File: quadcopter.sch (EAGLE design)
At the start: 66 parts, among them J1 AVR_SPI_PRG_6NS, M1 MOTOR_PADS, M2 MOTOR_PADS, M3 MOTOR_PADS, M4 MOTOR_PADS, Q1 MOSFET_SOT-23, Q2 MOSFET_SOT-23, Q3 MOSFET_SOT-23, Q4 MOSFET_SOT-23, SW1 PUSHBUTTON_SMD-VERTICAL-1, U1 ATMEGA128RFA1, U2 IMU_LSM9DS1TR, Y1 16MHz

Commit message: Rename N0 net
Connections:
- net N$1 renamed C6
- net N$10 renamed M2
- net N$11 renamed C22
- net N$12 renamed BATT1
- net N$13 renamed M1
- net N$14 renamed M3
- net N$15 renamed C9
- net N$16 renamed D6
- net N$17 renamed C21
- net N$18 renamed C13
- net N$19 renamed C14
- net N$2 renamed C5
- net N$20 renamed C23
- net N$21 renamed M4
- net N$22 renamed D7
- net N$23 renamed C24
- net N$3 renamed RFP
- net N$4 renamed RFN
- net N$5 renamed C1
- net N$6 renamed C4
- net N$7 renamed C2
- net N$8 renamed C3
- net N$9 renamed D5
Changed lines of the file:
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@@
 </segment>
 </net>
-<net name="N$3" class="0">
+<net name="RFP" class="0">
 <segment>
 <pinref part="U1" gate="G$1" pin="RFP"/>
@@
 </segment>
 </net>
-<net name="N$4" class="0">
-<segment>
-<pinref part="U1" gate="G$1" pin="RFN"/>
-<wire x1="200.66" y1="157.48" x2="218.44" y2="157.48" width="0.1524" layer="91"/>
-<wire x1="218.44" y1="157.48" x2="218.44" y2="149.86" width="0.1524" layer="91"/>
-<wire x1="218.44" y1="149.86" x2="236.22" y2="149.86" width="0.1524" layer="91"/>
-<wire x1="236.22" y1="149.86" x2="236.22" y2="152.4" width="0.1524" layer="91"/>
-<pinref part="B1" gate="G$1" pin="OUT2"/>
-</segment>
-</net>
-<net name="N$5" class="0">
+<net name="C1" class="0">
 <segment>
 <pinref part="B1" gate="G$1" pin="GND@2"/>
@@
 </segment>
 </net>
-<net name="N$7" class="0">
+<net name="C2" class="0">
 <segment>
 <pinref part="B1" gate="G$1" pin="IN"/>
@@
 </segment>
 </net>
-<net name="N$1" class="0">
+<net name="C6" class="0">
 <segment>
 <pinref part="U1" gate="G$1" pin="AVDD"/>
@@
 </segment>
 </net>
-<net name="N$2" class="0">
+<net name="C5" class="0">
 <segment>
 <pinref part="U1" gate="G$1" pin="DVDD"/>
@@
 </segment>
 </net>
-<net name="N$6" class="0">
+<net name="C4" class="0">
 <segment>
 <pinref part="U1" gate="G$1" pin="XTAL1"/>
@@
 </segment>
 </net>
-<net name="N$8" class="0">
+<net name="C3" class="0">
 <segment>
 <pinref part="U1" gate="G$1" pin="XTAL2"/>
@@
 </segment>
 </net>
-<net name="N$15" class="0">
+<net name="C9" class="0">
 <segment>
 <pinref part="JP1" gate="G$1" pin="1"/>
@@
 </segment>
 </net>
-<net name="N$18" class="0">
+<net name="C13" class="0">
 <segment>
 <pinref part="U2" gate="G$1" pin="CAP"/>
@@
 </segment>
 </net>
-<net name="N$19" class="0">
+<net name="C14" class="0">
 <segment>
 <pinref part="U2" gate="G$1" pin="C1"/>
@@
 </segment>
 </net>
-<net name="N$12" class="0">
+<net name="BATT1" class="0">
 <segment>
 <pinref part="J2" gate="G$1" pin="1"/>
@@
 </segment>
 </net>
-<net name="N$13" class="0">
+<net name="M1" class="0">
 <segment>
 <pinref part="M1" gate="G$1" pin="V-"/>
@@
 </segment>
 </net>
-<net name="N$17" class="0">
+<net name="C21" class="0">
 <segment>
 <pinref part="Q1" gate="G$1" pin="G"/>
@@
 </segment>
 </net>
-<net name="N$10" class="0">
+<net name="M2" class="0">
 <segment>
 <pinref part="M2" gate="G$1" pin="V-"/>
@@
 </segment>
 </net>
-<net name="N$11" class="0">
+<net name="C22" class="0">
 <segment>
 <pinref part="Q2" gate="G$1" pin="G"/>
@@
 </segment>
 </net>
-<net name="N$14" class="0">
+<net name="M3" class="0">
 <segment>
 <pinref part="M3" gate="G$1" pin="V-"/>
@@
 </segment>
 </net>
-<net name="N$20" class="0">
+<net name="C23" class="0">
 <segment>
 <pinref part="Q3" gate="G$1" pin="G"/>
@@
 </segment>
 </net>
-<net name="N$21" class="0">
+<net name="M4" class="0">
 <segment>
 <pinref part="M4" gate="G$1" pin="V-"/>
@@
 </segment>
 </net>
-<net name="N$23" class="0">
+<net name="C24" class="0">
 <segment>
 <pinref part="Q4" gate="G$1" pin="G"/>
@@
 </segment>
 </net>
-<net name="N$9" class="0">
+<net name="D5" class="0">
 <segment>
 <pinref part="R12" gate="G$1" pin="1"/>
@@
 </segment>
 </net>
-<net name="N$16" class="0">
+<net name="D6" class="0">
 <segment>
 <pinref part="R13" gate="G$1" pin="1"/>
@@
 </segment>
 </net>
-<net name="N$22" class="0">
+<net name="D7" class="0">
 <segment>
 <pinref part="R14" gate="G$1" pin="1"/>
@@
 </segment>
 </net>
+<net name="RFN" class="0">
+<segment>
+<pinref part="U1" gate="G$1" pin="RFN"/>
+<wire x1="200.66" y1="157.48" x2="218.44" y2="157.48" width="0.1524" layer="91"/>
+<wire x1="218.44" y1="157.48" x2="218.44" y2="149.86" width="0.1524" layer="91"/>
+<wire x1="218.44" y1="149.86" x2="236.22" y2="149.86" width="0.1524" layer="91"/>
+<pinref part="B1" gate="G$1" pin="OUT2"/>
+<wire x1="236.22" y1="149.86" x2="236.22" y2="152.4" width="0.1524" layer="91"/>
+</segment>
+</net>

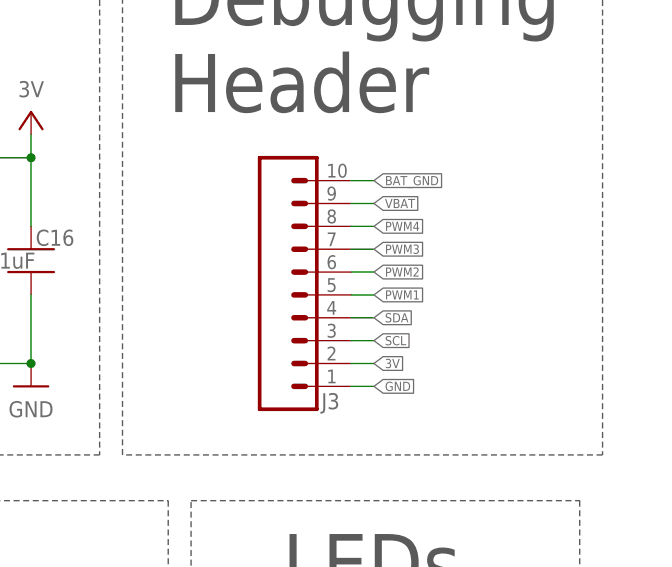
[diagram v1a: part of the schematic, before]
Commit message: Placed some parts on the board
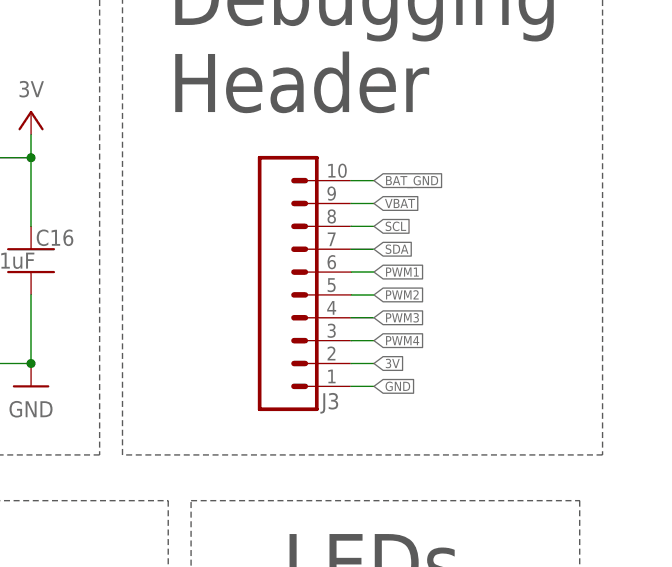
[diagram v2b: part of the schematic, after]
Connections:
- net PWM1: now also J3.6; no longer J3.5
- net PWM2: now also J3.5; no longer J3.6
- net PWM3: now also J3.4; no longer J3.7
- net PWM4: now also J3.3; no longer J3.8
- net SCL: now also J3.8; no longer J3.3
- net SDA: now also J3.7; no longer J3.4
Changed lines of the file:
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@@
 </segment>
 <segment>
-<pinref part="J3" gate="G$1" pin="8"/>
-<wire x1="375.92" y1="187.96" x2="378.46" y2="187.96" width="0.1524" layer="91"/>
-<label x="378.46" y="187.96" size="1.016" layer="95" xref="yes"/>
+<pinref part="J3" gate="G$1" pin="3"/>
+<wire x1="375.92" y1="175.26" x2="378.46" y2="175.26" width="0.1524" layer="91"/>
+<label x="378.46" y="175.26" size="1.016" layer="95" xref="yes"/>
 </segment>
 </net>
@@
 </segment>
 <segment>
-<pinref part="J3" gate="G$1" pin="3"/>
-<wire x1="375.92" y1="175.26" x2="378.46" y2="175.26" width="0.1524" layer="91"/>
-<label x="378.46" y="175.26" size="1.016" layer="95" xref="yes"/>
+<pinref part="J3" gate="G$1" pin="8"/>
+<wire x1="375.92" y1="187.96" x2="378.46" y2="187.96" width="0.1524" layer="91"/>
+<label x="378.46" y="187.96" size="1.016" layer="95" xref="yes"/>
 </segment>
 </net>
@@
 </segment>
 <segment>
+<pinref part="J3" gate="G$1" pin="7"/>
+<wire x1="375.92" y1="185.42" x2="378.46" y2="185.42" width="0.1524" layer="91"/>
+<label x="378.46" y="185.42" size="1.016" layer="95" xref="yes"/>
+</segment>
+</net>
+<net name="RXD0" class="0">
+<segment>
+<pinref part="U1" gate="G$1" pin="PE0(RXD0/PCINT8)"/>
+<wire x1="144.78" y1="132.08" x2="142.24" y2="132.08" width="0.1524" layer="91"/>
+<label x="142.24" y="132.08" size="1.016" layer="95" rot="R180" xref="yes"/>
+</segment>
+<segment>
+<pinref part="JP1" gate="G$1" pin="3"/>
+<wire x1="157.48" y1="78.74" x2="160.02" y2="78.74" width="0.1524" layer="91"/>
+<label x="160.02" y="78.74" size="1.016" layer="95" xref="yes"/>
+</segment>
+</net>
+<net name="TXD0" class="0">
+<segment>
+<pinref part="U1" gate="G$1" pin="PE1(TXD0)"/>
+<wire x1="144.78" y1="129.54" x2="142.24" y2="129.54" width="0.1524" layer="91"/>
+<label x="142.24" y="129.54" size="1.016" layer="95" rot="R180" xref="yes"/>
+</segment>
+<segment>
+<pinref part="JP1" gate="G$1" pin="2"/>
+<wire x1="157.48" y1="81.28" x2="160.02" y2="81.28" width="0.1524" layer="91"/>
+<label x="160.02" y="81.28" size="1.016" layer="95" xref="yes"/>
+</segment>
+</net>
+<net name="PWM3" class="0">
+<segment>
+<pinref part="U1" gate="G$1" pin="PE5(OC3C/INT5)"/>
+<wire x1="144.78" y1="119.38" x2="142.24" y2="119.38" width="0.1524" layer="91"/>
+<label x="142.24" y="119.38" size="1.016" layer="95" rot="R180" xref="yes"/>
+</segment>
+<segment>
+<pinref part="R8" gate="G$1" pin="1"/>
+<wire x1="38.1" y1="116.84" x2="35.56" y2="116.84" width="0.1524" layer="91"/>
+<label x="35.56" y="116.84" size="1.016" layer="95" rot="R180" xref="yes"/>
+</segment>
+<segment>
 <pinref part="J3" gate="G$1" pin="4"/>
 <wire x1="375.92" y1="177.8" x2="378.46" y2="177.8" width="0.1524" layer="91"/>
 <label x="378.46" y="177.8" size="1.016" layer="95" xref="yes"/>
-</segment>
-</net>
-<net name="RXD0" class="0">
-<segment>
-<pinref part="U1" gate="G$1" pin="PE0(RXD0/PCINT8)"/>
-<wire x1="144.78" y1="132.08" x2="142.24" y2="132.08" width="0.1524" layer="91"/>
-<label x="142.24" y="132.08" size="1.016" layer="95" rot="R180" xref="yes"/>
-</segment>
-<segment>
-<pinref part="JP1" gate="G$1" pin="3"/>
-<wire x1="157.48" y1="78.74" x2="160.02" y2="78.74" width="0.1524" layer="91"/>
-<label x="160.02" y="78.74" size="1.016" layer="95" xref="yes"/>
-</segment>
-</net>
-<net name="TXD0" class="0">
-<segment>
-<pinref part="U1" gate="G$1" pin="PE1(TXD0)"/>
-<wire x1="144.78" y1="129.54" x2="142.24" y2="129.54" width="0.1524" layer="91"/>
-<label x="142.24" y="129.54" size="1.016" layer="95" rot="R180" xref="yes"/>
-</segment>
-<segment>
-<pinref part="JP1" gate="G$1" pin="2"/>
-<wire x1="157.48" y1="81.28" x2="160.02" y2="81.28" width="0.1524" layer="91"/>
-<label x="160.02" y="81.28" size="1.016" layer="95" xref="yes"/>
-</segment>
-</net>
-<net name="PWM3" class="0">
-<segment>
-<pinref part="U1" gate="G$1" pin="PE5(OC3C/INT5)"/>
-<wire x1="144.78" y1="119.38" x2="142.24" y2="119.38" width="0.1524" layer="91"/>
-<label x="142.24" y="119.38" size="1.016" layer="95" rot="R180" xref="yes"/>
-</segment>
-<segment>
-<pinref part="R8" gate="G$1" pin="1"/>
-<wire x1="38.1" y1="116.84" x2="35.56" y2="116.84" width="0.1524" layer="91"/>
-<label x="35.56" y="116.84" size="1.016" layer="95" rot="R180" xref="yes"/>
-</segment>
-<segment>
-<pinref part="J3" gate="G$1" pin="7"/>
-<wire x1="375.92" y1="185.42" x2="378.46" y2="185.42" width="0.1524" layer="91"/>
-<label x="378.46" y="185.42" size="1.016" layer="95" xref="yes"/>
 </segment>
 </net>
@@
 </segment>
 <segment>
-<pinref part="J3" gate="G$1" pin="5"/>
-<wire x1="375.92" y1="180.34" x2="378.46" y2="180.34" width="0.1524" layer="91"/>
-<label x="378.46" y="180.34" size="1.016" layer="95" xref="yes"/>
+<pinref part="J3" gate="G$1" pin="6"/>
+<wire x1="375.92" y1="182.88" x2="378.46" y2="182.88" width="0.1524" layer="91"/>
+<label x="378.46" y="182.88" size="1.016" layer="95" xref="yes"/>
 </segment>
 </net>
@@
 </segment>
 <segment>
-<pinref part="J3" gate="G$1" pin="6"/>
-<wire x1="375.92" y1="182.88" x2="378.46" y2="182.88" width="0.1524" layer="91"/>
-<label x="378.46" y="182.88" size="1.016" layer="95" xref="yes"/>
-</segment>
-</net>
+<pinref part="J3" gate="G$1" pin="5"/>
+<wire x1="375.92" y1="180.34" x2="378.46" y2="180.34" width="0.1524" layer="91"/>
+<label x="378.46" y="180.34" size="1.016" layer="95" xref="yes"/>
+</segment>
+</net>

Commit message: Finished board design
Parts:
- added V1, V10, V11, V12, V13, V14, V15, V16, V17, V18, V19, V2, V20, V21, V22, V23, V24, V25, V26, V27, V28, V29, V3, V30, V31, V32, V33, V4, V5, V6, V7, V8, V9: (no value), quadparts_prebuilt:LOCKED-VIA-0.254
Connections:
- net 3V: now also V1.N, V2.N, V3.N, V32.N, V4.N
- net BAT_GND: now also V5.N, V6.N, V7.N, V8.N
- net GND: now also V13.N, V14.N, V15.N, V16.N, V17.N, V18.N, V19.N, V20.N, V21.N, V22.N, V23.N, V24.N, V25.N, V26.N, V27.N, V28.N, V29.N, V30.N, V31.N, V33.N
- net VBAT: now also V10.N, V11.N, V12.N, V9.N
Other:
- note added: "VIAs"
- moved on the sheet: C10, C11, C12, C13, C14, D5, D6, D7, R12, R13, R14, R2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

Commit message: Modified board design
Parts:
- removed V2, V4: (no value), quadparts_prebuilt:LOCKED-VIA-0.254
- added V34: (no value), quadparts_prebuilt:LOCKED-VIA-0.254
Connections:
- net 3V: no longer V2.N, V4.N
- net GND: now also V34.N
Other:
- moved on the sheet: V3, V32
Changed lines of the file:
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@@
 <?xml version="1.0" encoding="utf-8"?>
 <!DOCTYPE eagle SYSTEM "eagle.dtd">
-<eagle version="9.0.0">
+<eagle version="8.7.1">
 <drawing>
 <settings>
-<setting alwaysvectorfont="no"/>
+<setting alwaysvectorfont="yes"/>
 <setting verticaltext="up"/>
 </settings>
-<grid distance="0.1" unitdist="inch" unit="inch" style="dots" multiple="1" display="yes" altdistance="0.01" altunitdist="inch" altunit="inch"/>
+<grid distance="0.1" unitdist="inch" unit="inch" style="lines" multiple="1" display="no" altdistance="0.01" altunitdist="inch" altunit="inch"/>
 <layers>
 <layer number="1" name="Top" color="4" fill="1" visible="no" active="no"/>
@@
 <part name="GND21" library="quadparts_prebuilt" deviceset="BAT_GND" device=""/>
 <part name="V1" library="quadparts_prebuilt" deviceset="LOCKED-VIA" device="-0.254"/>
-<part name="V2" library="quadparts_prebuilt" deviceset="LOCKED-VIA" device="-0.254"/>
 <part name="V3" library="quadparts_prebuilt" deviceset="LOCKED-VIA" device="-0.254"/>
-<part name="V4" library="quadparts_prebuilt" deviceset="LOCKED-VIA" device="-0.254"/>
 <part name="P+15" library="quadparts_prebuilt" deviceset="3V" device=""/>
 <part name="V5" library="quadparts_prebuilt" deviceset="LOCKED-VIA" device="-0.254"/>
@@
 <part name="V32" library="quadparts_prebuilt" deviceset="LOCKED-VIA" device="-0.254"/>
 <part name="V33" library="quadparts_prebuilt" deviceset="LOCKED-VIA" device="-0.254"/>
+<part name="V34" library="quadparts_prebuilt" deviceset="LOCKED-VIA" device="-0.254"/>
 </parts>
 <sheets>
@@
 <instance part="GND21" gate="1" x="391.16" y="109.22"/>
 <instance part="V1" gate="G$1" x="30.48" y="68.58" rot="R270"/>
-<instance part="V2" gate="G$1" x="35.56" y="68.58" rot="R270"/>
-<instance part="V3" gate="G$1" x="40.64" y="68.58" rot="R270"/>
-<instance part="V4" gate="G$1" x="45.72" y="68.58" rot="R270"/>
+<instance part="V3" gate="G$1" x="33.02" y="68.58" rot="R270"/>
 <instance part="P+15" gate="G$1" x="30.48" y="73.66"/>
 <instance part="V5" gate="G$1" x="30.48" y="33.02" rot="R90"/>
@@
 <instance part="V30" gate="G$1" x="119.38" y="30.48" rot="R90"/>
 <instance part="V31" gate="G$1" x="124.46" y="30.48" rot="R90"/>
-<instance part="V32" gate="G$1" x="38.1" y="68.58" rot="R90"/>
+<instance part="V32" gate="G$1" x="35.56" y="68.58" rot="R270"/>
 <instance part="V33" gate="G$1" x="106.68" y="30.48" rot="R270"/>
+<instance part="V34" gate="G$1" x="111.76" y="30.48" rot="R270"/>
 </instances>
 <busses>
@@
 <pinref part="P+15" gate="G$1" pin="3V"/>
 <wire x1="30.48" y1="71.12" x2="30.48" y2="68.58" width="0.1524" layer="91"/>
-<pinref part="V2" gate="G$1" pin="N"/>
-<wire x1="30.48" y1="68.58" x2="35.56" y2="68.58" width="0.1524" layer="91"/>
+<pinref part="V3" gate="G$1" pin="N"/>
+<wire x1="30.48" y1="68.58" x2="33.02" y2="68.58" width="0.1524" layer="91"/>
 <junction x="30.48" y="68.58"/>
-<pinref part="V3" gate="G$1" pin="N"/>
-<wire x1="35.56" y1="68.58" x2="38.1" y2="68.58" width="0.1524" layer="91"/>
-<junction x="35.56" y="68.58"/>
-<pinref part="V4" gate="G$1" pin="N"/>
-<wire x1="38.1" y1="68.58" x2="40.64" y2="68.58" width="0.1524" layer="91"/>
-<wire x1="40.64" y1="68.58" x2="45.72" y2="68.58" width="0.1524" layer="91"/>
-<junction x="40.64" y="68.58"/>
 <pinref part="V32" gate="G$1" pin="N"/>
-<junction x="38.1" y="68.58"/>
+<wire x1="33.02" y1="68.58" x2="35.56" y2="68.58" width="0.1524" layer="91"/>
+<junction x="33.02" y="68.58"/>
 </segment>
 </net>
@@
 <pinref part="V19" gate="G$1" pin="N"/>
 <wire x1="119.38" y1="30.48" x2="114.3" y2="30.48" width="0.1524" layer="91"/>
-<wire x1="114.3" y1="30.48" x2="109.22" y2="30.48" width="0.1524" layer="91"/>
+<wire x1="114.3" y1="30.48" x2="111.76" y2="30.48" width="0.1524" layer="91"/>
+<wire x1="111.76" y1="30.48" x2="109.22" y2="30.48" width="0.1524" layer="91"/>
 <wire x1="109.22" y1="30.48" x2="106.68" y2="30.48" width="0.1524" layer="91"/>
 <wire x1="106.68" y1="30.48" x2="104.14" y2="30.48" width="0.1524" layer="91"/>
@@
 <pinref part="V33" gate="G$1" pin="N"/>
 <junction x="106.68" y="30.48"/>
-</segment>
-</net>
+<pinref part="V34" gate="G$1" pin="N"/>
+<junction x="111.76" y="30.48"/>
+</segment>
+</net>
